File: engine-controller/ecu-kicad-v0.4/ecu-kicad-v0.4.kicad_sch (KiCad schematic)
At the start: 0 parts

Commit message: Changed ECU v0.4 to use more fused outputs
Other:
- sheet Ethernet ports: added ETH_CRS_DV, ETH_LED_GREEN, ETH_LED_YELLOW, ETH_MDC, ETH_MDIO, ETH_REF_CLK, ETH_RX+, ETH_RX-, ETH_RXD0, ETH_RXD1, ETH_TX+, ETH_TX-, ETH_TXD0, ETH_TXD1, ETH_TXEN; removed none
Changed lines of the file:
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@@
 (kicad_sch (version 20230121) (generator eeschema)
   (paper "A2")
-  (sheet (at 125.73 74.93) (size 73.66 38.1) (fields_autoplaced)
+  (sheet (at 368.3 277.495) (size 73.66 38.1) (fields_autoplaced)
     (stroke (width 0.1524) (type solid))
     (fill (color 0 0 0 0.0000))
-    (property "Sheetname" "Output Driving" (at 125.73 74.2184 0)
+    (property "Sheetname" "Output Driving" (at 368.3 276.7834 0)
       (effects (font (size 1.27 1.27)) (justify left bottom))
     )
-    (property "Sheetfile" "driving.kicad_sch" (at 125.73 113.6146 0)
+    (property "Sheetfile" "driving.kicad_sch" (at 368.3 316.1796 0)
       (effects (font (size 1.27 1.27)) (justify left top))
     )
@@
     )
   )
-  (sheet (at 210.82 73.66) (size 80.01 38.1) (fields_autoplaced)
+  (sheet (at 356.87 160.655) (size 80.01 38.1) (fields_autoplaced)
     (stroke (width 0.1524) (type solid))
     (fill (color 0 0 0 0.0000))
-    (property "Sheetname" "Temperature" (at 210.82 72.9484 0)
+    (property "Sheetname" "Temperature" (at 356.87 159.9434 0)
       (effects (font (size 1.27 1.27)) (justify left bottom))
     )
-    (property "Sheetfile" "temperature.kicad_sch" (at 210.82 112.3446 0)
+    (property "Sheetfile" "temperature.kicad_sch" (at 356.87 199.3396 0)
       (effects (font (size 1.27 1.27)) (justify left top))
     )
@@
     )
   )
-  (sheet (at 125.73 25.4) (size 73.66 40.64) (fields_autoplaced)
+  (sheet (at 368.3 227.965) (size 73.66 40.64) (fields_autoplaced)
     (stroke (width 0.1524) (type solid))
     (fill (color 0 0 0 0.0000))
-    (property "Sheetname" "Microcontroller" (at 125.73 24.6884 0)
+    (property "Sheetname" "Microcontroller" (at 368.3 227.2534 0)
       (effects (font (size 1.27 1.27)) (justify left bottom))
     )
-    (property "Sheetfile" "microcontroller.kicad_sch" (at 125.73 66.6246 0)
+    (property "Sheetfile" "microcontroller.kicad_sch" (at 368.3 269.1896 0)
       (effects (font (size 1.27 1.27)) (justify left top))
     )
@@
     )
   )
-  (sheet (at 302.26 73.66) (size 78.105 36.83) (fields_autoplaced)
+  (sheet (at 448.31 160.655) (size 78.105 36.83) (fields_autoplaced)
     (stroke (width 0.1524) (type solid))
     (fill (color 0 0 0 0.0000))
-    (property "Sheetname" "Pressure" (at 302.26 72.9484 0)
+    (property "Sheetname" "Pressure" (at 448.31 159.9434 0)
       (effects (font (size 1.27 1.27)) (justify left bottom))
     )
-    (property "Sheetfile" "pressure.kicad_sch" (at 302.26 111.0746 0)
+    (property "Sheetfile" "pressure.kicad_sch" (at 448.31 198.0696 0)
       (effects (font (size 1.27 1.27)) (justify left top))
     )
@@
     )
   )
-  (sheet (at 209.55 27.94) (size 83.82 36.83) (fields_autoplaced)
+  (sheet (at 194.31 76.2) (size 38.1 38.1) (fields_autoplaced)
     (stroke (width 0.1524) (type solid))
     (fill (color 0 0 0 0.0000))
-    (property "Sheetname" "Ethernet" (at 209.55 27.2284 0)
+    (property "Sheetname" "Ethernet" (at 194.31 75.4884 0)
       (effects (font (size 1.27 1.27)) (justify left bottom))
     )
-    (property "Sheetfile" "ethernet.kicad_sch" (at 209.55 65.3546 0)
+    (property "Sheetfile" "ethernet.kicad_sch" (at 194.31 114.8846 0)
       (effects (font (size 1.27 1.27)) (justify left top))
     )
+    (pin "ETH_MDIO" bidirectional (at 194.31 85.725 180)
+      (effects (font (size 1.27 1.27)) (justify left))
+    )
+    (pin "ETH_MDC" input (at 194.31 87.63 180)
+      (effects (font (size 1.27 1.27)) (justify left))
+    )
+    (pin "ETH_REF_CLK" output (at 194.31 89.535 180)
+      (effects (font (size 1.27 1.27)) (justify left))
+    )
+    (pin "ETH_TXEN" input (at 194.31 91.44 180)
+      (effects (font (size 1.27 1.27)) (justify left))
+    )
+    (pin "ETH_TXD0" input (at 194.31 93.345 180)
+      (effects (font (size 1.27 1.27)) (justify left))
+    )
+    (pin "ETH_TXD1" input (at 194.31 95.25 180)
+      (effects (font (size 1.27 1.27)) (justify left))
+    )
+    (pin "ETH_CRS_DV" output (at 194.31 97.155 180)
+      (effects (font (size 1.27 1.27)) (justify left))
+    )
+    (pin "ETH_RXD0" output (at 194.31 99.06 180)
+      (effects (font (size 1.27 1.27)) (justify left))
+    )
+    (pin "ETH_RXD1" output (at 194.31 100.965 180)
+      (effects (font (size 1.27 1.27)) (justify left))
+    )
+    (pin "ETH_LED_YELLOW" output (at 194.31 104.775 180)
+      (effects (font (size 1.27 1.27)) (justify left))
+    )
+    (pin "ETH_LED_GREEN" output (at 194.31 106.68 180)
+      (effects (font (size 1.27 1.27)) (justify left))
+    )
+    (pin "ETH_RX+" output (at 232.41 91.44 0)
+      (effects (font (size 1.27 1.27)) (justify right))
+    )
+    (pin "ETH_TX+" output (at 232.41 93.345 0)
+      (effects (font (size 1.27 1.27)) (justify right))
+    )
+    (pin "ETH_RX-" output (at 232.41 95.25 0)
+      (effects (font (size 1.27 1.27)) (justify right))
+    )
+    (pin "ETH_TX-" output (at 232.41 97.155 0)
+      (effects (font (size 1.27 1.27)) (justify right))
+    )
     (instances

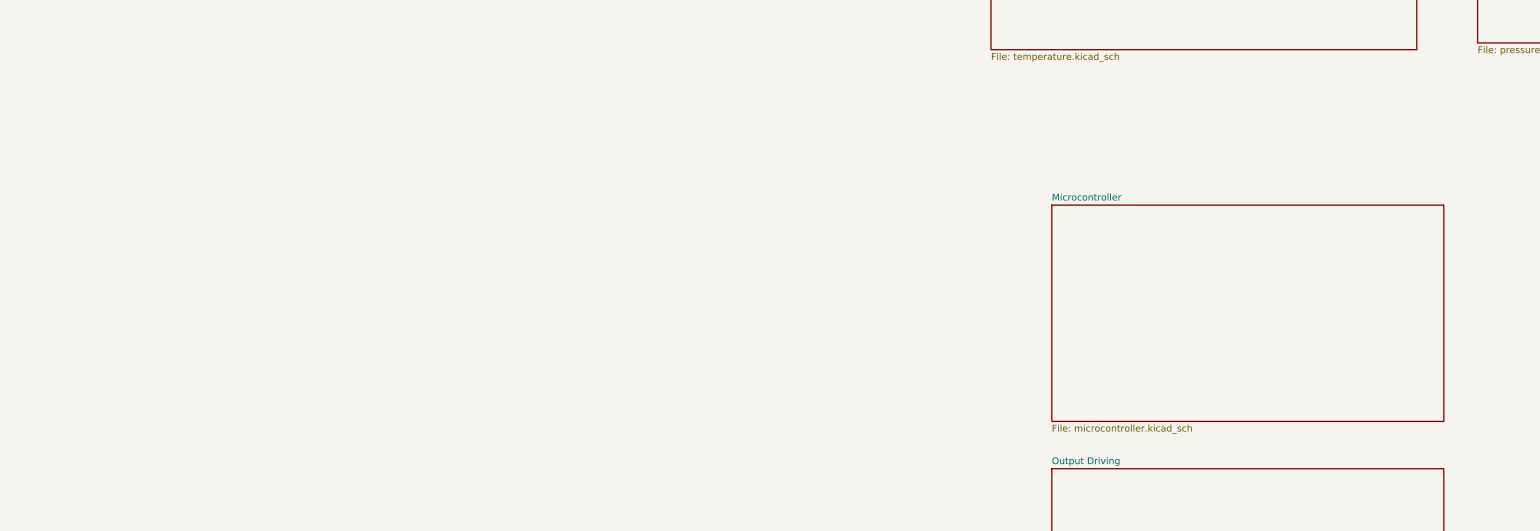
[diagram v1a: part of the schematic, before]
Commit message: Better sim configs + ecu v0.4 work
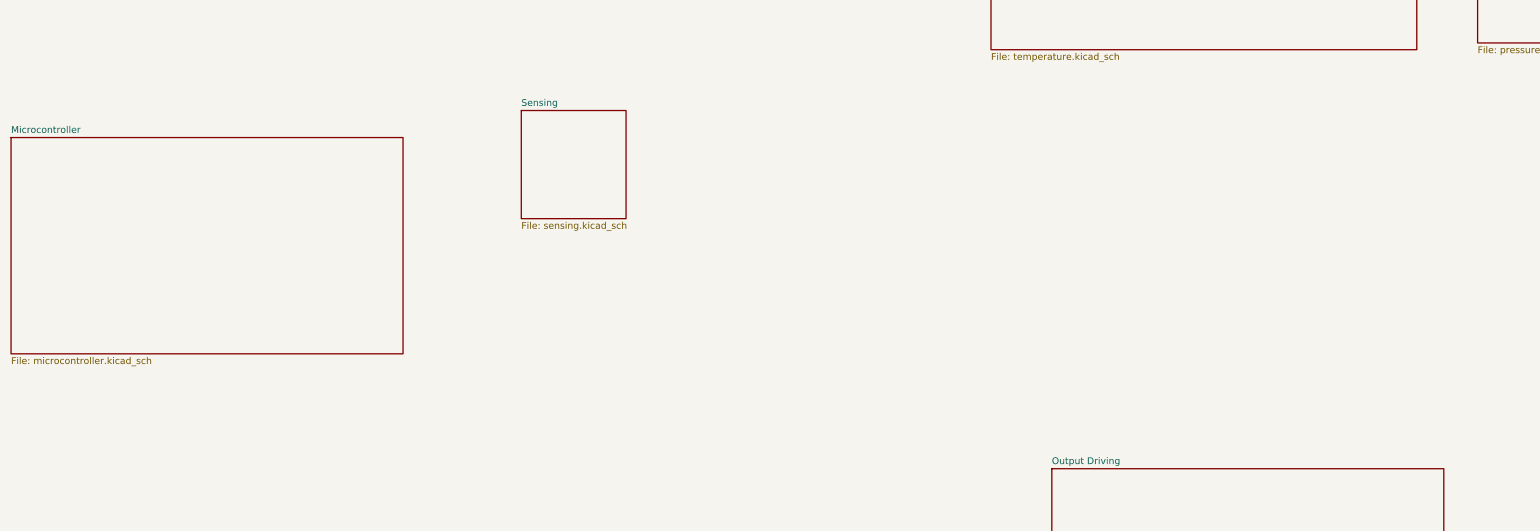
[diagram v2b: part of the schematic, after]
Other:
- added sheet Sensing (sensing.kicad_sch)
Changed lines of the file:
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@@
 (kicad_sch (version 20230121) (generator eeschema)
   (paper "A2")
+  (sheet (at 268.605 210.185) (size 19.685 20.32) (fields_autoplaced)
+    (stroke (width 0.1524) (type solid))
+    (fill (color 0 0 0 0.0000))
+    (property "Sheetname" "Sensing" (at 268.605 209.4734 0)
+      (effects (font (size 1.27 1.27)) (justify left bottom))
+    )
+    (property "Sheetfile" "sensing.kicad_sch" (at 268.605 231.0896 0)
+      (effects (font (size 1.27 1.27)) (justify left top))
+    )
+    (instances
+      (project "ecu-kicad-v0.4"
+        (path "/36cc65d2-4dd3-4f51-bcce-4252e60c9ae8" (page "11"))
+      )
+    )
+  )
   (sheet (at 368.3 277.495) (size 73.66 38.1) (fields_autoplaced)
     (stroke (width 0.1524) (type solid))
@@
     )
   )
-  (sheet (at 368.3 227.965) (size 73.66 40.64) (fields_autoplaced)
+  (sheet (at 172.72 215.265) (size 73.66 40.64) (fields_autoplaced)
     (stroke (width 0.1524) (type solid))
     (fill (color 0 0 0 0.0000))
-    (property "Sheetname" "Microcontroller" (at 368.3 227.2534 0)
+    (property "Sheetname" "Microcontroller" (at 172.72 214.5534 0)
       (effects (font (size 1.27 1.27)) (justify left bottom))
     )
-    (property "Sheetfile" "microcontroller.kicad_sch" (at 368.3 269.1896 0)
+    (property "Sheetfile" "microcontroller.kicad_sch" (at 172.72 256.4896 0)
       (effects (font (size 1.27 1.27)) (justify left top))
     )

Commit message: Lots of sim changes oof
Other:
- removed sheet Pressure
- removed sheet Temperature
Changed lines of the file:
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@@
-    )
-  )
-  (sheet (at 356.87 160.655) (size 80.01 38.1) (fields_autoplaced)
-    (stroke (width 0.1524) (type solid))
-    (fill (color 0 0 0 0.0000))
-    (property "Sheetname" "Temperature" (at 356.87 159.9434 0)
-      (effects (font (size 1.27 1.27)) (justify left bottom))
-    )
-    (property "Sheetfile" "temperature.kicad_sch" (at 356.87 199.3396 0)
-      (effects (font (size 1.27 1.27)) (justify left top))
-    )
-    (instances
-      (project "ecu-kicad-v0.4"
-        (path "/36cc65d2-4dd3-4f51-bcce-4252e60c9ae8" (page "5"))
-      )
     )
   )
@@
       )
     )
-  )
-  (sheet (at 448.31 160.655) (size 78.105 36.83) (fields_autoplaced)
-    (stroke (width 0.1524) (type solid))
-    (fill (color 0 0 0 0.0000))
-    (property "Sheetname" "Pressure" (at 448.31 159.9434 0)
-      (effects (font (size 1.27 1.27)) (justify left bottom))
-    )
-    (property "Sheetfile" "pressure.kicad_sch" (at 448.31 198.0696 0)
-      (effects (font (size 1.27 1.27)) (justify left top))
-    )
-    (instances
-      (project "ecu-kicad-v0.4"
-        (path "/36cc65d2-4dd3-4f51-bcce-4252e60c9ae8" (page "6"))
-      )
-    )

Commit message: Progress on ECU v0.4
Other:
- sheet Sensing ports: added TEMP_SEL0, TEMP_SEL1, TEMP_SEL2, TEMP_SEL3, THERM_IN; removed none
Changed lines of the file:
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@@
 (kicad_sch (version 20230121) (generator eeschema)
-  (paper "A2")
+  (paper "A3")
   (sheet (at 268.605 210.185) (size 19.685 20.32) (fields_autoplaced)
     (stroke (width 0.1524) (type solid))
@@
     (property "Sheetfile" "sensing.kicad_sch" (at 268.605 231.0896 0)
       (effects (font (size 1.27 1.27)) (justify left top))
+    )
+    (pin "TEMP_SEL0" input (at 268.605 213.36 180)
+      (effects (font (size 1.27 1.27)) (justify left))
+    )
+    (pin "TEMP_SEL1" input (at 268.605 215.9 180)
+      (effects (font (size 1.27 1.27)) (justify left))
+    )
+    (pin "TEMP_SEL3" input (at 268.605 218.44 180)
+      (effects (font (size 1.27 1.27)) (justify left))
+    )
+    (pin "TEMP_SEL2" input (at 268.605 223.52 180)
+      (effects (font (size 1.27 1.27)) (justify left))
+    )
+    (pin "THERM_IN" input (at 268.605 226.06 180)
+      (effects (font (size 1.27 1.27)) (justify left))
     )
     (instances
@@
     )
   )
-  (sheet (at 172.72 215.265) (size 73.66 40.64) (fields_autoplaced)
+  (sheet (at 156.21 144.145) (size 41.91 65.405) (fields_autoplaced)
     (stroke (width 0.1524) (type solid))
     (fill (color 0 0 0 0.0000))
-    (property "Sheetname" "Microcontroller" (at 172.72 214.5534 0)
+    (property "Sheetname" "Microcontroller" (at 156.21 143.4334 0)
       (effects (font (size 1.27 1.27)) (justify left bottom))
     )
-    (property "Sheetfile" "microcontroller.kicad_sch" (at 172.72 256.4896 0)
+    (property "Sheetfile" "microcontroller.kicad_sch" (at 156.21 210.1346 0)
       (effects (font (size 1.27 1.27)) (justify left top))
     )
